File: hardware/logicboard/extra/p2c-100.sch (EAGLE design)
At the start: 49 parts, among them IC1 74LS07N, K1 G5V1, T1 2SC1815, U1 MKR1000

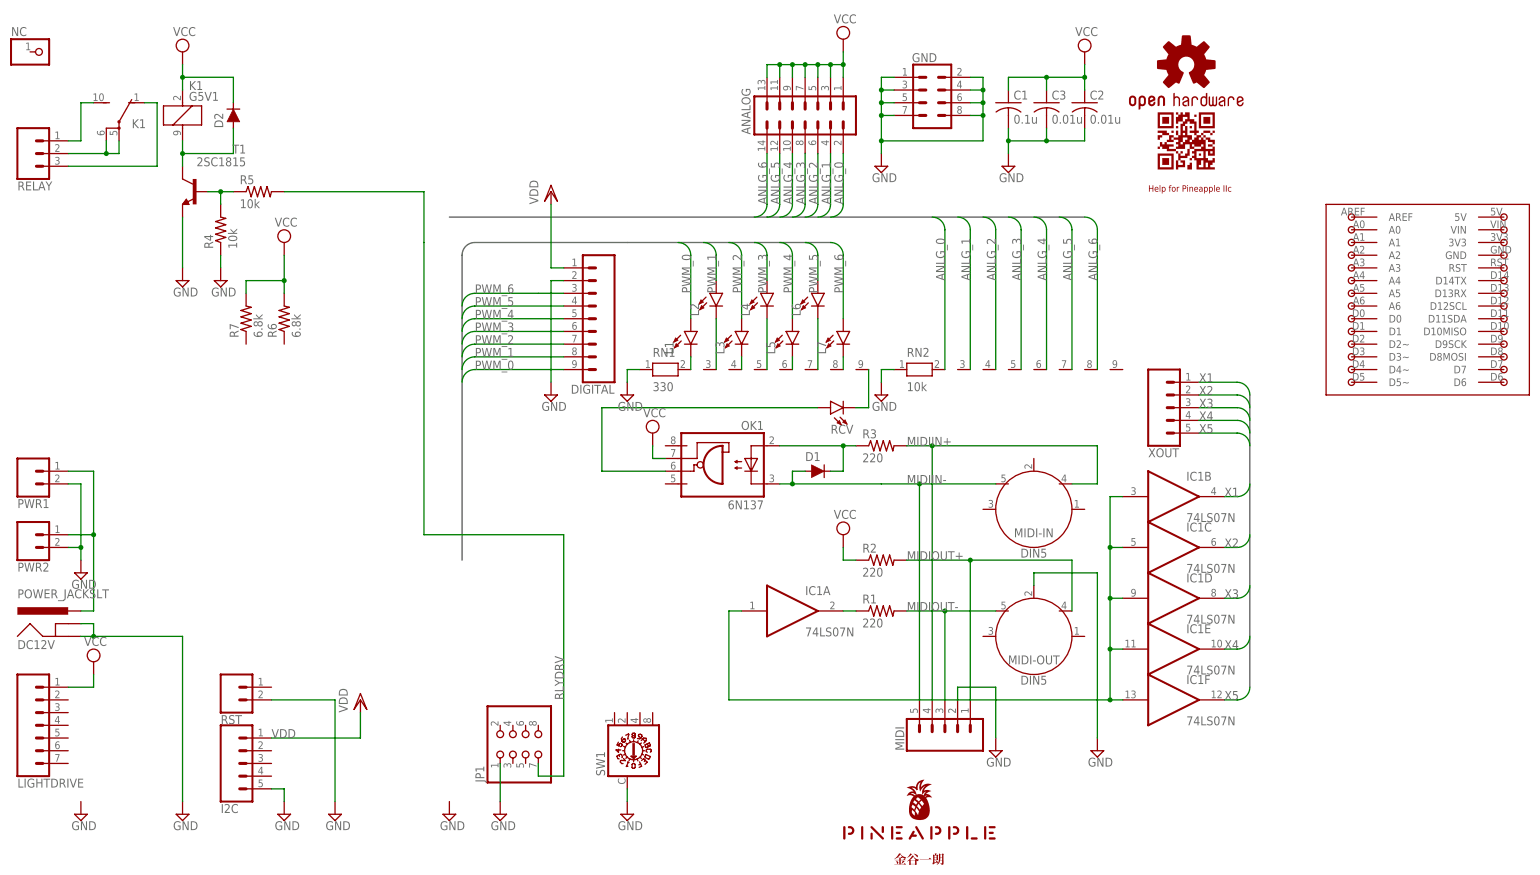
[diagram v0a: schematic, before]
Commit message: Test of MKR1000 version.
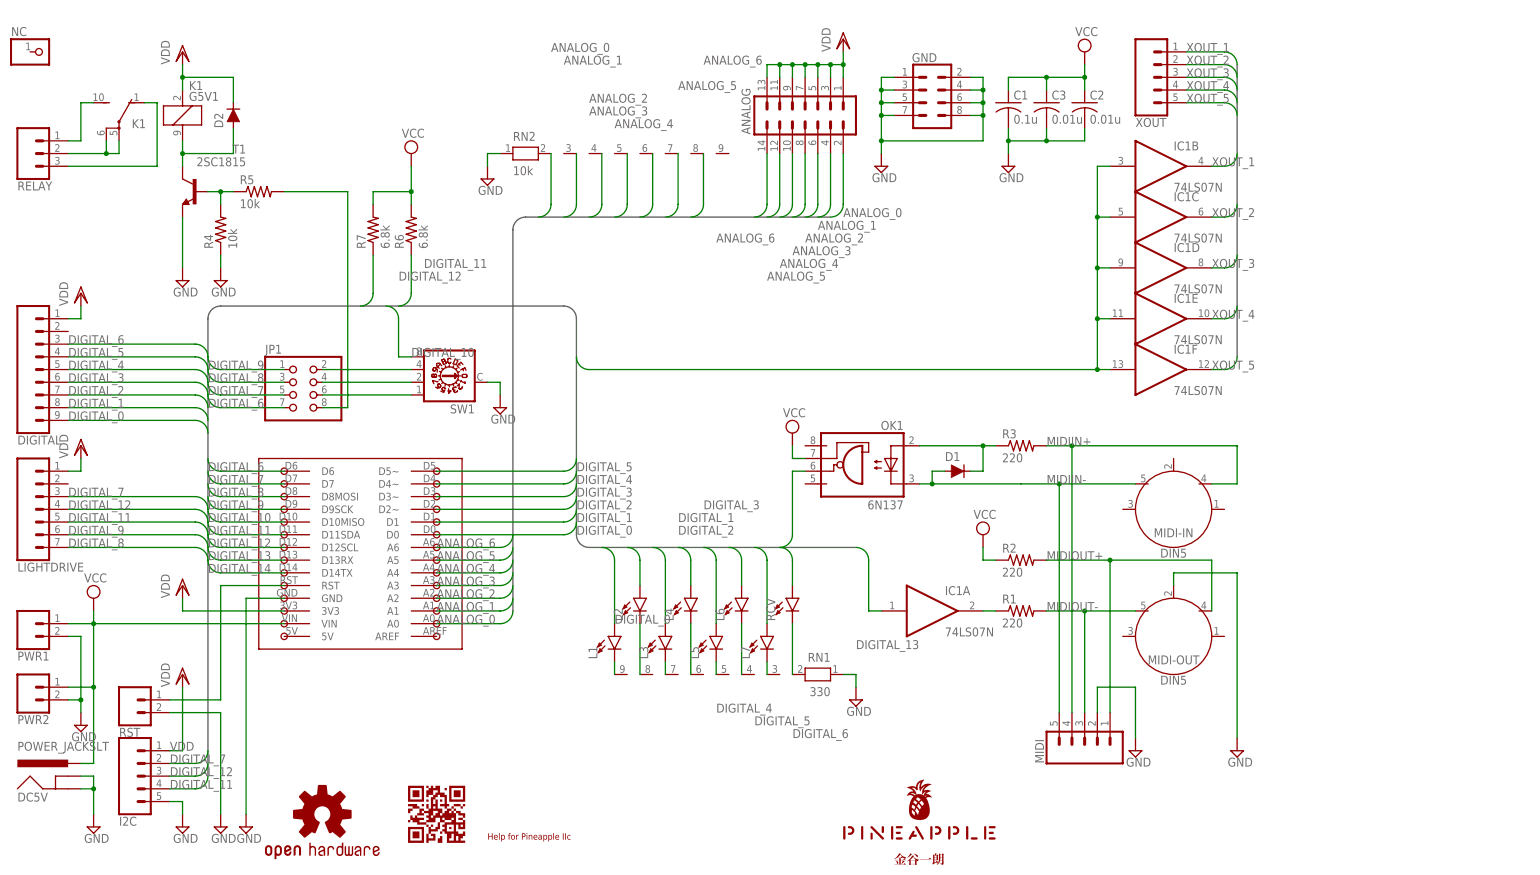
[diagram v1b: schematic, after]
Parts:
- removed DC12V: POWER_JACKSLT, SparkFun-Connectors:POWER_JACKSLT
- added DC5V: POWER_JACKSLT, SparkFun-Connectors:POWER_JACKSLT
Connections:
- net X1 renamed XOUT_1
- net X2 renamed XOUT_2
- net X3 renamed XOUT_3
- net X4 renamed XOUT_4
- net X5 renamed XOUT_5
- removed net ANLG_0: ANALOG.2, RN2.2
- removed net ANLG_1: ANALOG.4, RN2.3
- removed net ANLG_2: ANALOG.6, RN2.4
- removed net ANLG_3: ANALOG.8, RN2.5
- removed net ANLG_4: ANALOG.10, RN2.6
- removed net ANLG_5: ANALOG.12, RN2.7
- removed net ANLG_6: ANALOG.14, RN2.8
- removed net LED1K: L1.C, RN1.2
- removed net LED2K: L2.C, RN1.3
- removed net LED3K: L3.C, RN1.4
- removed net LED4K: L4.C, RN1.5
- removed net LED5K: L5.C, RN1.6
- removed net LED6K: L6.C, RN1.7
- removed net LED7K: L7.C, RN1.8
- removed net MIDIIN: OK1.VO, RCV.A
- removed net MIDIOUT: IC1A.I, IC1B.I, IC1C.I, IC1D.I, IC1E.I, IC1F.I
- removed net PWM_0: DIGITAL.9, L1.A
- removed net PWM_1: DIGITAL.8, L2.A
- removed net PWM_2: DIGITAL.7, L3.A
- removed net PWM_3: DIGITAL.6, L4.A
- removed net PWM_4: DIGITAL.5, L5.A
- removed net PWM_5: DIGITAL.4, L6.A
- removed net PWM_6: DIGITAL.3, L7.A
- removed net RLYDRV: JP1.7, R5.2
- removed net VIN: DC12V.PWR, PWR1.1, PWR2.1
- new net ANALOG_0: ANALOG.2, RN2.2, U1.A0
- new net ANALOG_1: ANALOG.4, RN2.3, U1.A1
- new net ANALOG_2: ANALOG.6, RN2.4, U1.A2
- new net ANALOG_3: ANALOG.8, RN2.5, U1.A3
- new net ANALOG_4: ANALOG.10, RN2.6, U1.A4
- new net ANALOG_5: ANALOG.12, RN2.7, U1.A5
- new net ANALOG_6: ANALOG.14, RN2.8, U1.A6
- new net DIGITAL_0: DIGITAL.9, L1.A, U1.D0
- new net DIGITAL_1: DIGITAL.8, L2.A, U1.D1
- new net DIGITAL_10: SW1.8, U1.D10MISO
- new net DIGITAL_11: I2C.4, LIGHTDRIVE.5, R6.1, U1.D11SDA
- new net DIGITAL_12: I2C.3, LIGHTDRIVE.4, R7.1, U1.D12SCL
- new net DIGITAL_13: OK1.VO, RCV.A, U1.D13RX
- new net DIGITAL_14: IC1A.I, IC1B.I, IC1C.I, IC1D.I, IC1E.I, IC1F.I, U1.D14TX
- new net DIGITAL_2: DIGITAL.7, L3.A, U1.D2~
- new net DIGITAL_3: DIGITAL.6, L4.A, U1.D3~
- new net DIGITAL_4: DIGITAL.5, L5.A, U1.D4~
- new net DIGITAL_5: DIGITAL.4, L6.A, U1.D5~
- new net DIGITAL_6: DIGITAL.3, JP1.7, L7.A, U1.D6
- new net DIGITAL_7: I2C.2, JP1.5, LIGHTDRIVE.3, U1.D7
- new net DIGITAL_8: JP1.3, LIGHTDRIVE.7, U1.D8MOSI
- new net DIGITAL_9: JP1.1, LIGHTDRIVE.6, U1.D9SCK
- new net N$10: L5.C, RN1.5
- new net N$11: L6.C, RN1.4
- new net N$12: L7.C, RN1.3
- new net N$13: RCV.C, RN1.2
- new net N$2: RST.1, U1.RST
- new net N$3: JP1.8, R5.2
- new net N$4: JP1.6, SW1.1
- new net N$5: JP1.4, SW1.2
- new net N$6: JP1.2, SW1.4
- new net N$7: L2.C, RN1.8
- new net N$8: L3.C, RN1.7
- new net N$9: L4.C, RN1.6
- net GND: now also DC5V.GND, DC5V.GNDBREAK, U1.GND; no longer DC12V.GND, DC12V.GNDBREAK, DIGITAL.2, JP1.1
- net N$1: now also L1.C; no longer RCV.C
- net VCC: now also DC5V.PWR, PWR1.1, PWR2.1, U1.VIN; no longer ANALOG.1, ANALOG.11, ANALOG.13, ANALOG.3, ANALOG.5, ANALOG.7, ANALOG.9, D2.C, K11.1, LIGHTDRIVE.1
- net VDD: now also ANALOG.1, ANALOG.11, ANALOG.13, ANALOG.3, ANALOG.5, ANALOG.7, ANALOG.9, D2.C, K11.1, LIGHTDRIVE.1, U1.3V3
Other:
- moved on the sheet: D1, DIGITAL, I2C, IC1A, IC1B, IC1C, IC1D, IC1E, IC1F, JP1, L1, L2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
